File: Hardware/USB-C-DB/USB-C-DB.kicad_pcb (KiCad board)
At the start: 2 copper layers, 85.6 x 54 mm, 219 parts, among them J1 USB_C_Receptacle, J10 GND, J11 MCU_RST, J12 MCU_EN, J13 MCU_TOUT, J14 MCU_IO0, J15 EFUSE_PRG, J16 UART_DTRN, J17 UART_RTSN, J18 NOT_SUSP, J19 IBUS_S+, J2 EFPROG_POS, J20 IBUS_S-, J21 RESETN, J22 DEBUGGER, J23 +5V, J24 PWM_BC, J25 GND, J3 EFPROG_NEG, J4 BatTP+, J5 Battery con, J6 BatTP-, J7 P3V3, J8 VBUS, J9 FT_VCCIO, Q1 XP262N7002TR-G, Q10 XP262N7002TR-G, Q2 XP262N7002TR-G, Q3 XP262N7002TR-G, Q4 XP262N7002TR-G, Q5 XP262N7002TR-G, Q6 XP262N7002TR-G, Q7 XP262N7002TR-G, Q8 XP262N7002TR-G, Q9 XP262N7002TR-G, U1 NUF2221W1T2G, U10 NA555D, U2 LD1117S33TR_SOT223, U3 FT260S-U, U4 ESP-WROOM-02, U5 74HC595_mod, U6 74HC595, U7 74HC595, U8 74HC595, U9 74HC595

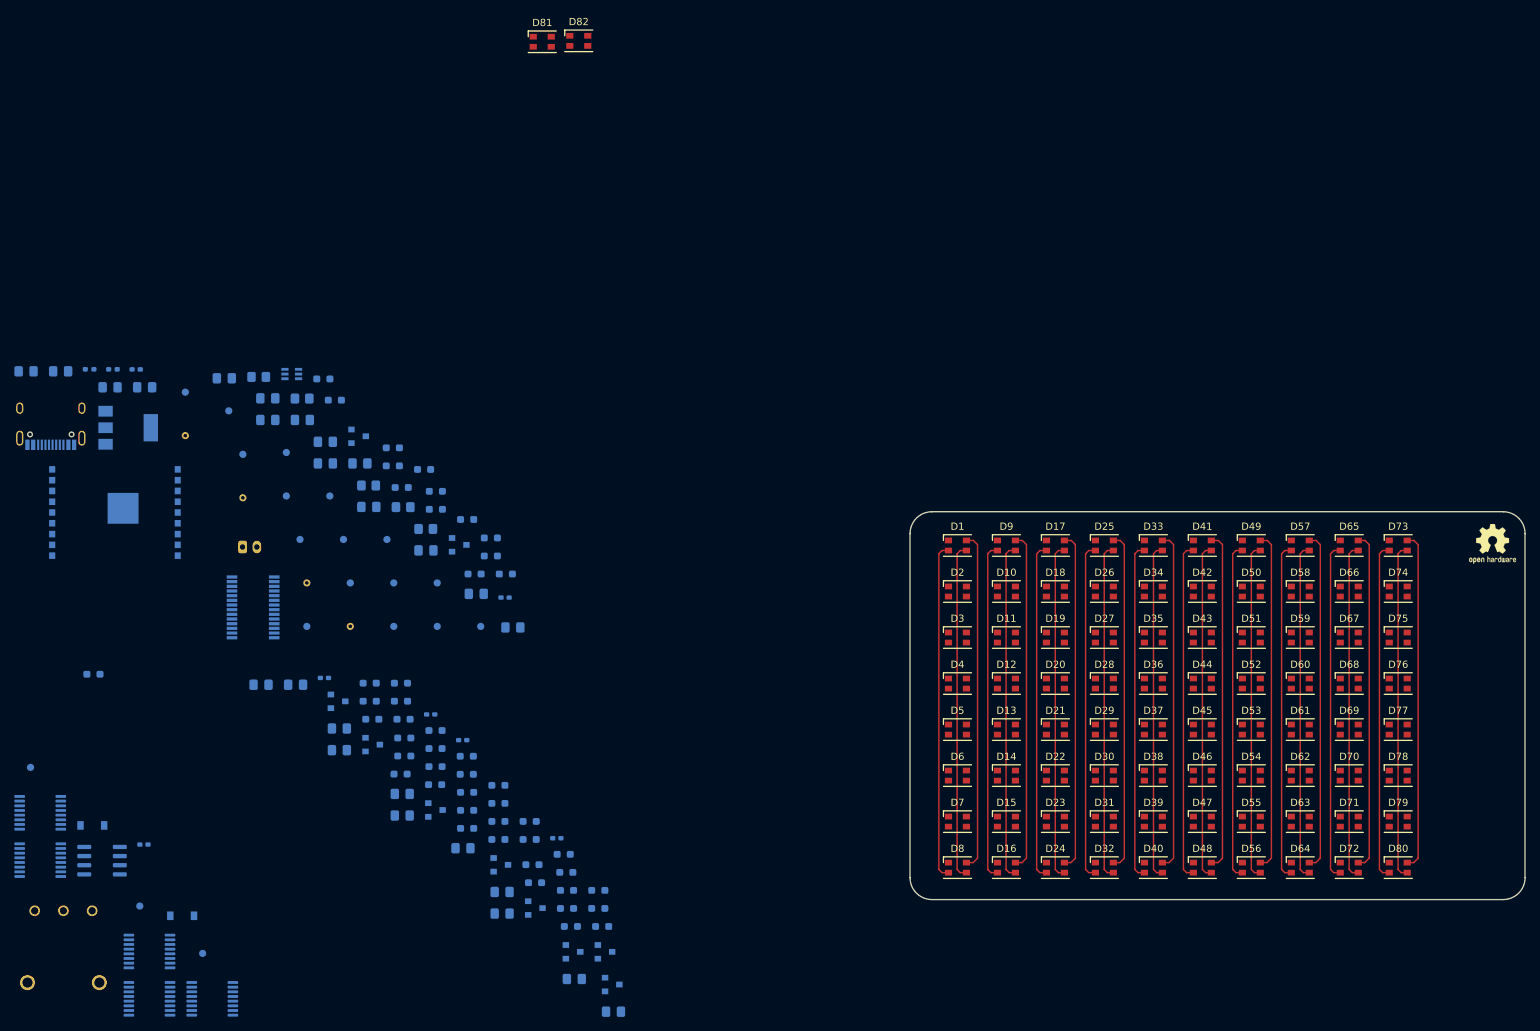
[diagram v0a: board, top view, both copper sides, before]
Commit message: Adding OSHW logo on PCB
* Updating BOM with available parts for test run
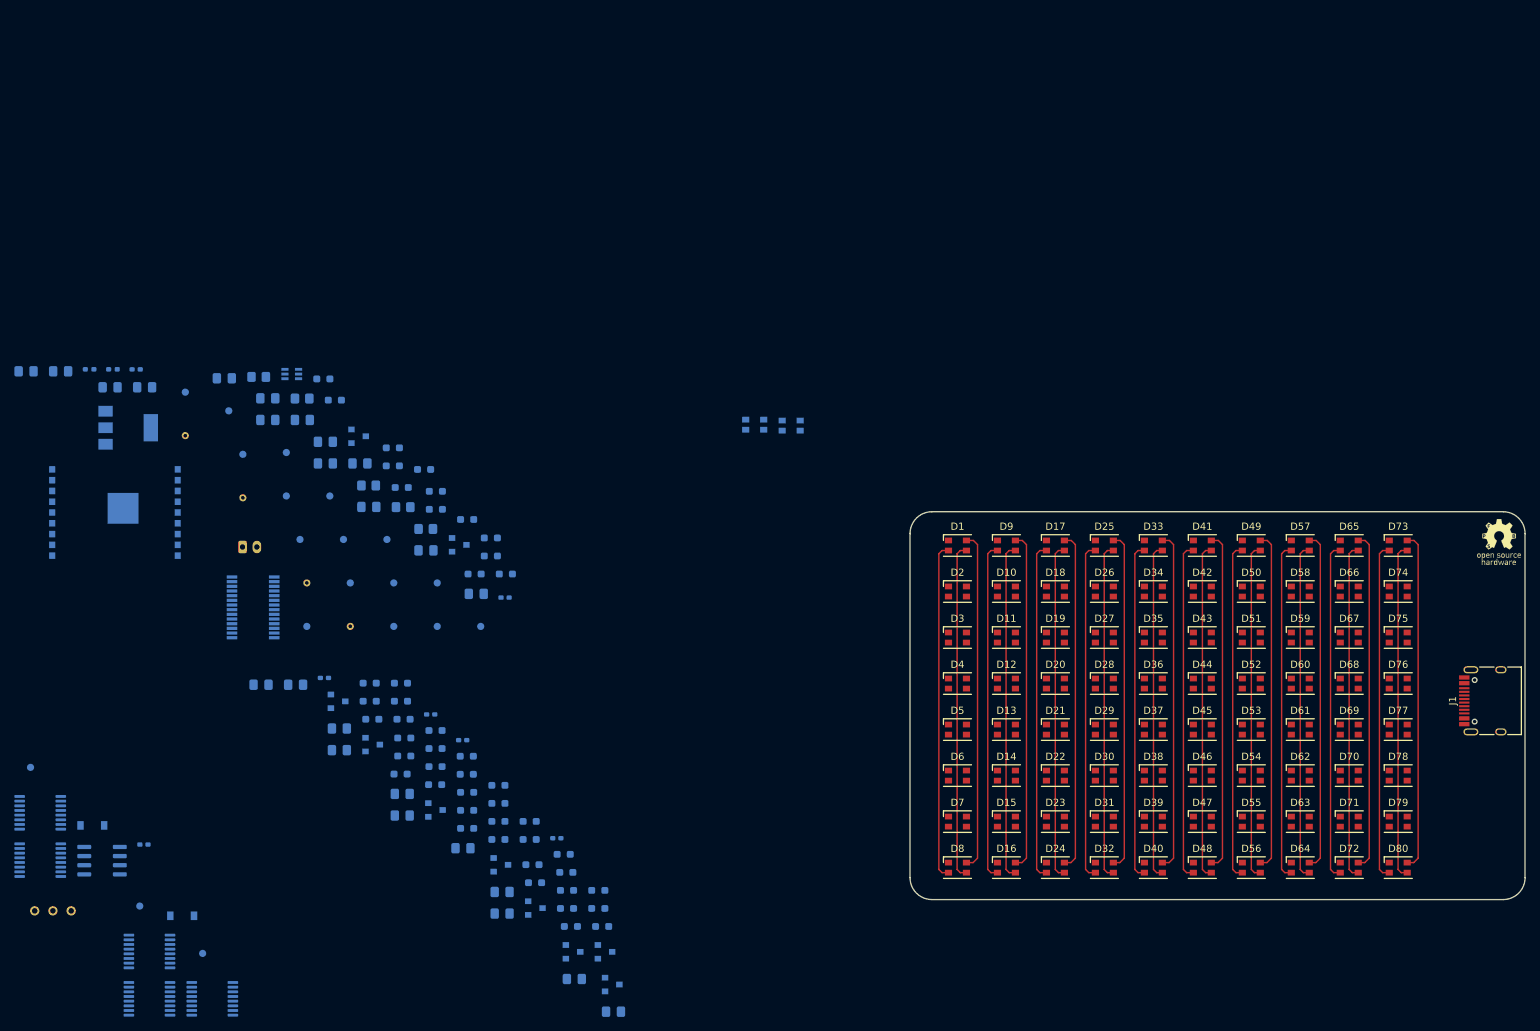
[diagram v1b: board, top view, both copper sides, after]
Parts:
- removed the C4 at (113.1, 117.7)
- removed the R7 at (54.8, 124.2)
- removed REF**: OSHW-Logo2_7.3x6mm_SilkScreen, Symbol:OSHW-Logo2_7.3x6mm_SilkScreen
- added G1: LOGO, USB-C-DB:oshw-spfb, F.Cu at (250.4, 105.8)
- C4: value 0.1u -> 10u
- D81, D82: moved to B.Cu
- J1: moved to F.Cu
- VR1: value RV100F-30-4K1-B1M -> 3352T-1-105LF; footprint Mouser-imports:RV100F304K1B1M -> Mouser-imports:3352T1103LF
- moved J1 204.6 mm to (249.6, 127.9), turned to 90 degrees
- moved D82 61.2 mm to (151.9, 89.6)
- moved D81 60.9 mm to (146.8, 89.5)
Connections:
- R7 pad 1: Net-(FB1-Pad1) -> /VBUS_ISEN+
- R7 pad 2: /VBUS_ISEN+ -> +5V

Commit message: Adding full layout for design
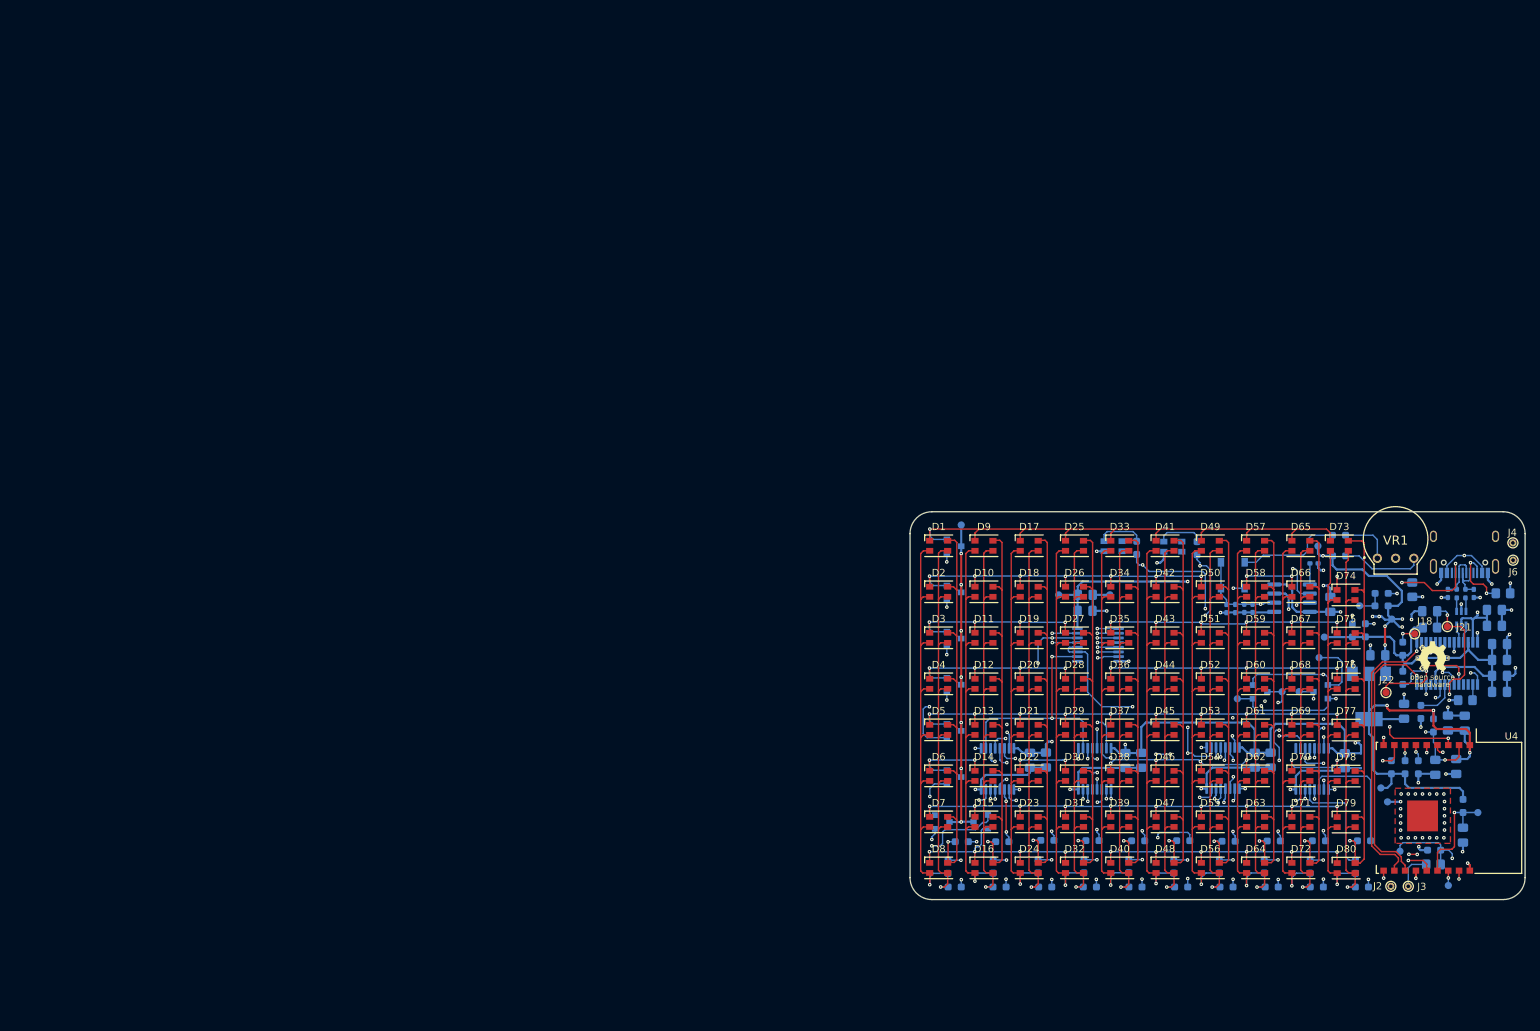
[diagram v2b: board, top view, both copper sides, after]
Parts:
- removed C26: 0.1u, Capacitor_SMD:C_0805_2012Metric_Pad1.18x1.45mm_HandSolder
- removed J5: Battery con, Connector_JST:JST_PH_B2B-PH-K_1x02_P2.00mm_Vertical
- J1: moved to B.Cu
- J18, J2, J21, J22, J3, J4, J6, U4, VR1: moved to F.Cu
- moved C12 203.8 mm to (243.3, 131.0), turned to 90 degrees
- moved C16 201.5 mm to (245.6, 131.0), turned to 90 degrees
- moved C14 198.3 mm to (245.4, 146.6), turned to 270 degrees
- moved VR1 193.2 mm to (233.4, 108.1)
- moved R9 192.8 mm to (244.5, 113.0), turned to 90 degrees
- moved R10 190.8 mm to (245.7, 113.0), turned to 90 degrees
- moved J11 189.2 mm to (247.4, 143.5)
- moved C1 188.8 mm to (246.9, 113.0), turned to 270 degrees
- moved C15 187.2 mm to (241.5, 137.2), turned to 270 degrees
- moved U4 187.1 mm to (240.3, 142.8), turned to 270 degrees
- moved J4 185.4 mm to (252.3, 105.9), turned to 180 degrees
- moved U9 177.5 mm to (224.4, 137.4), turned to 90 degrees
- moved J6 177.0 mm to (252.3, 108.3), turned to 180 degrees
- moved U2 176.7 mm to (232.3, 127.3), turned to 270 degrees
- moved C10 175.1 mm to (250.4, 124.4)
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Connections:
- net /UART_RX_N renamed /UART_TRX_N
- net /UART_TX_P renamed /UART_TRX_P
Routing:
- net +5V: track 0.00 -> 282.5 mm, vias 0 -> 14
- net /EOUT: track 0.00 -> 131.3 mm, vias 0 -> 8
- net GND: track 0.00 -> 119.9 mm, vias 0 -> 60
- net /MCU_IO5: track 0.00 -> 113.6 mm, vias 0 -> 5
- net /DATA: track 0.00 -> 109.0 mm, vias 0 -> 5
- net /MCU_IO13: track 0.00 -> 105.5 mm, vias 0 -> 6
- net /Display-and-controller-61B0EECC/PWM_BC: track 0.00 -> 102.4 mm, vias 0 -> 8
- net /DCLK: track 0.00 -> 93.5 mm, vias 0 -> 10
- net Net-(D14-Pad1): track 0.00 -> 80.5 mm, vias 0 -> 10
- net Net-(D1-Pad1): track 0.00 -> 77.1 mm, vias 0 -> 1
- net Net-(D16-Pad1): track 0.00 -> 75.9 mm, vias 0 -> 10
- net Net-(D10-Pad1): track 0.00 -> 75.5 mm, vias 0 -> 10
- net Net-(D11-Pad1): track 0.00 -> 75.2 mm, vias 0 -> 10
- net Net-(D12-Pad1): track 0.00 -> 75.0 mm, vias 0 -> 10
- net Net-(D13-Pad1): track 0.00 -> 74.9 mm, vias 0 -> 10
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- added copper zone on F.Cu, net GND
- added copper zone on In2.CuPWR, net GND
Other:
- copper layers 2 -> 4
- net class Default: clearance 0.2 -> 0.15; via_dia 0.8 -> 0.5; via_drill 0.4 -> 0.2
- net class Min (300mA): via_dia 0.8 -> 0.45; via_drill 0.4 -> 0.1
- net class Power (500mA): clearance 0.2 -> 0.15; via_dia 0.8 -> 0.5; via_drill 0.4 -> 0.2
- net class USB data added: clearance 0.1524, trace_width 0.2, via_dia 0.5, via_drill 0.2
- rule trace_clearance: 0.2 -> 0.15
- rule via_min_drill: 0.3 -> 0.1
- rule via_min_size: 0.8 -> 0.45

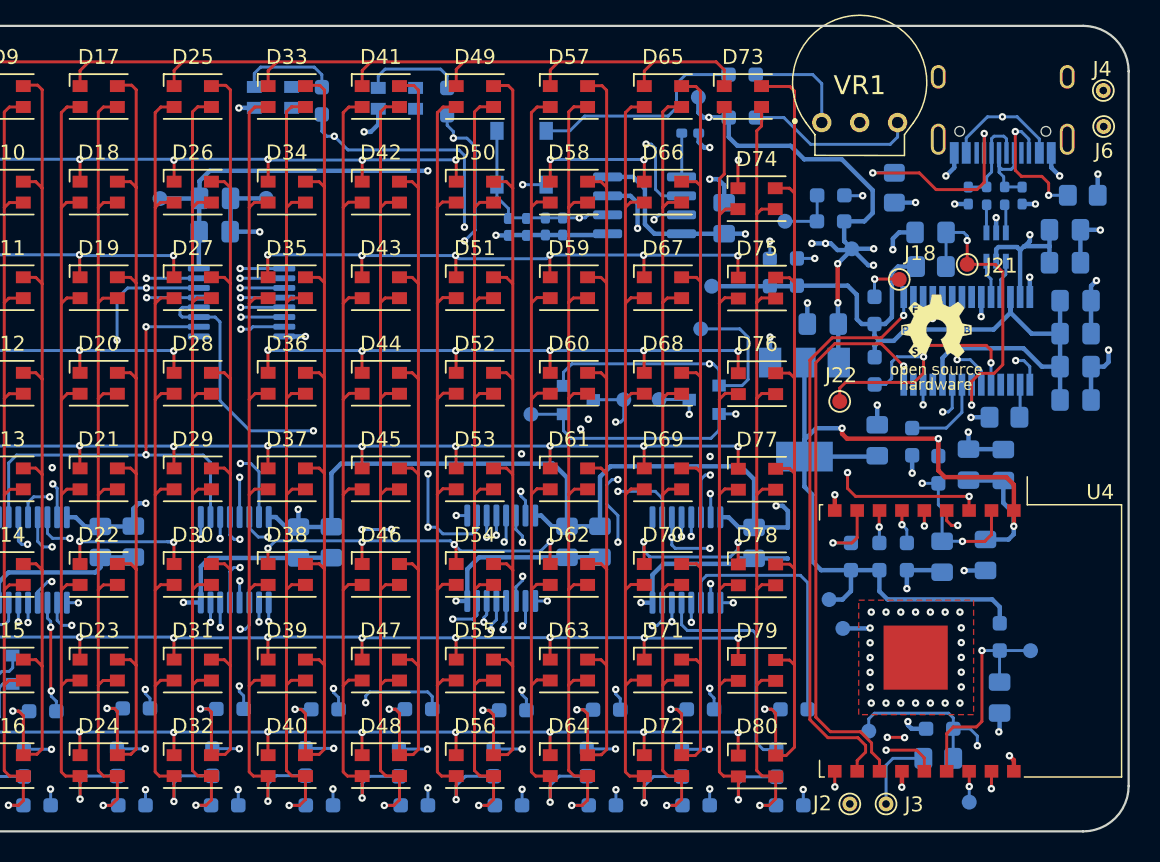
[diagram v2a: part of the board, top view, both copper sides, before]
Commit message: Updating layout with version info
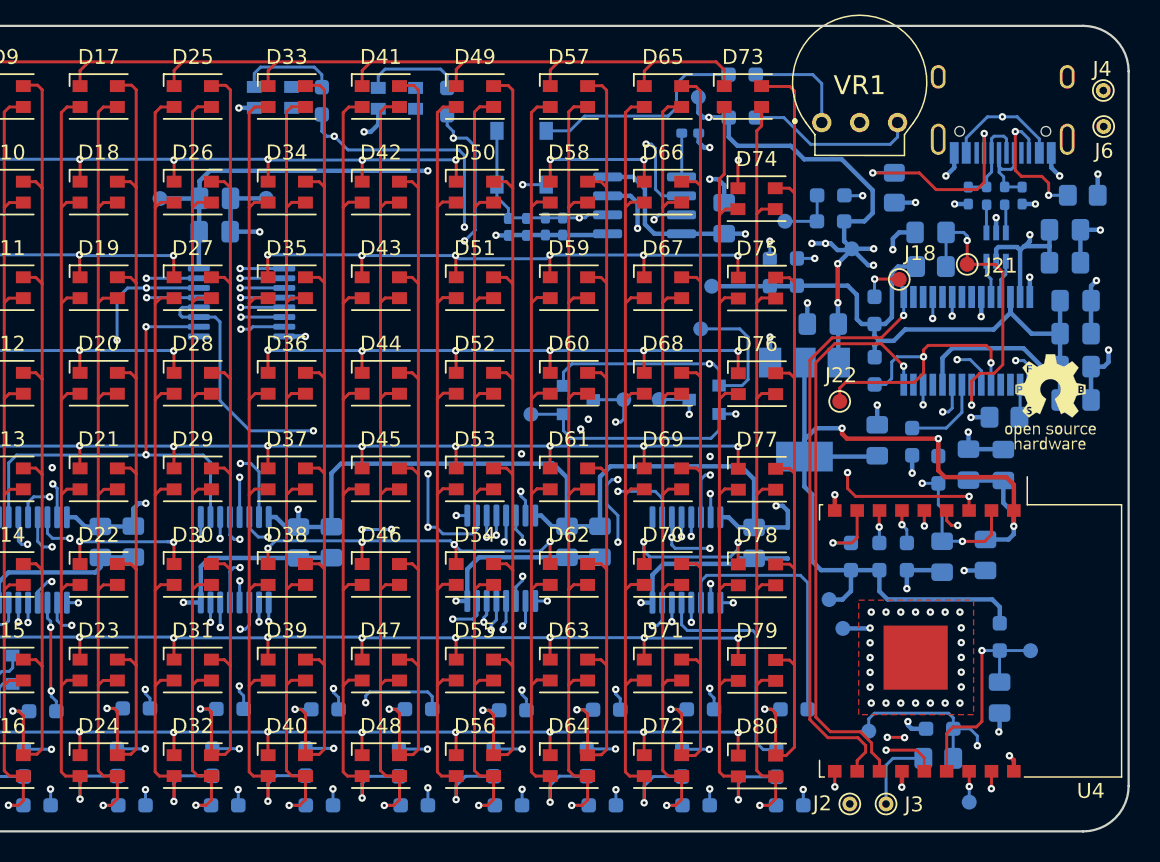
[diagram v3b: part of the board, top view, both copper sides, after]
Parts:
- moved G1 8.62 mm to (248.8, 126.8)
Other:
- board text added: "GitHub@Rr42 Rev: v0.6.1"
